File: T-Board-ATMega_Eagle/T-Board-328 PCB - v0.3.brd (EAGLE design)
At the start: 50.8 x 67.9 mm, 26 parts, among them IC1 LD117MIRROR, IC4 NCP1117MIRROR, J1 POWER_JACKPTH, J2 AVR_SPI_PRG_6PTH, U1 ATMEGA328P_PDIP

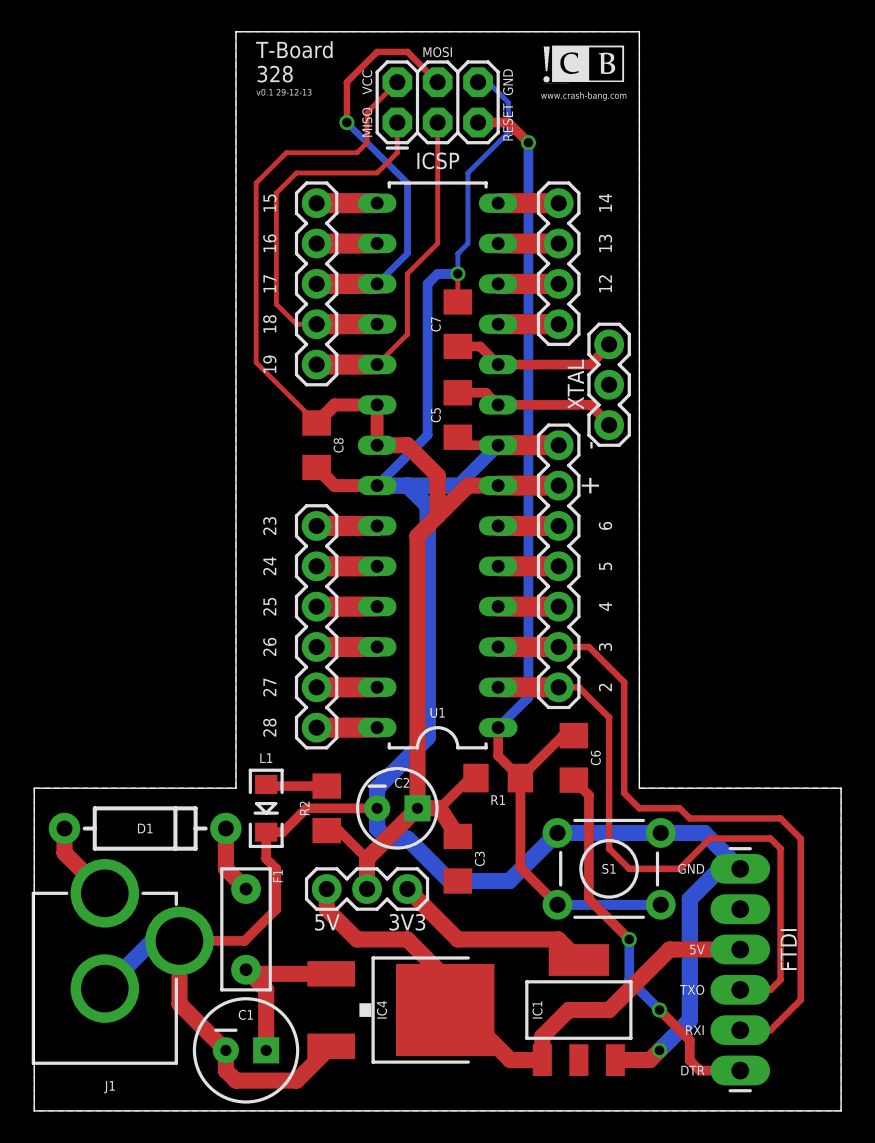
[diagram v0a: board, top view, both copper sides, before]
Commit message: v0.4 - Second Prototype
Second prototype sent to OSHPark for fab.
- Reduced footprint
- Corrected mirrored voltage regulators
- Corrected unconnected capacitor
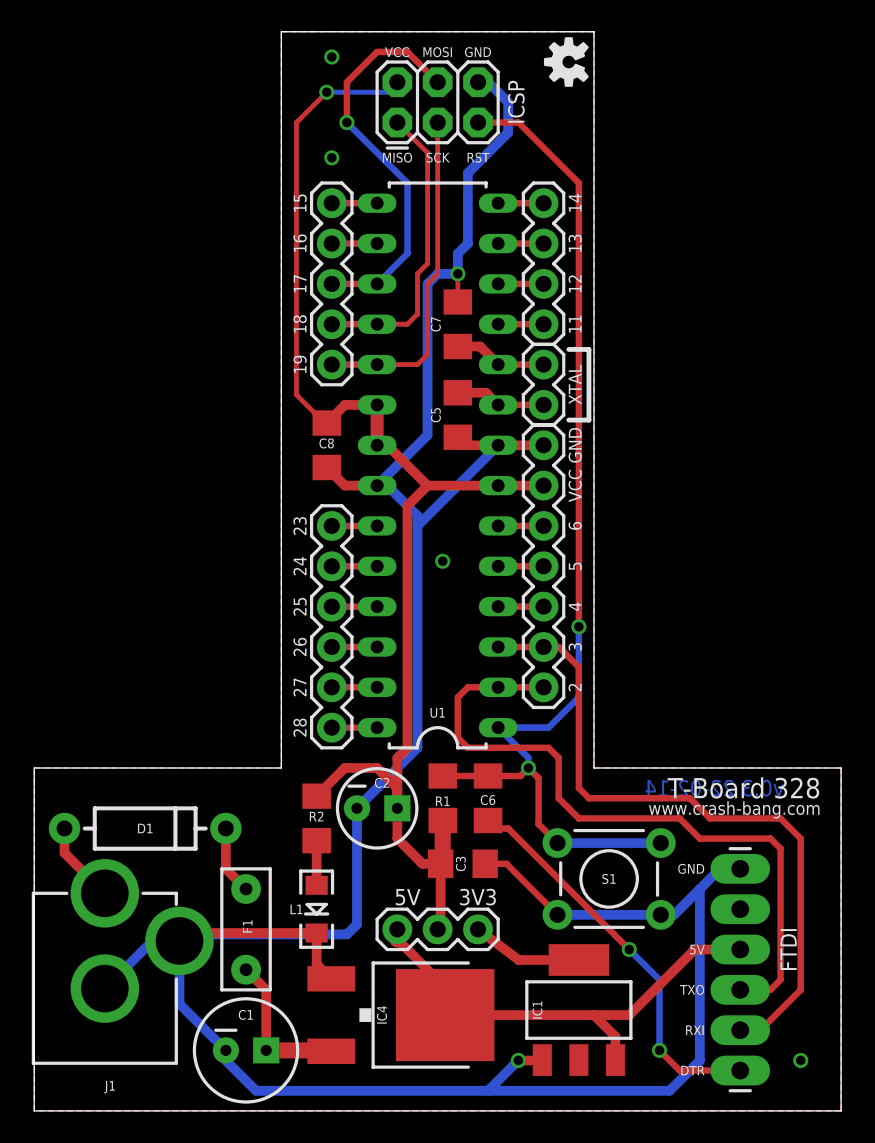
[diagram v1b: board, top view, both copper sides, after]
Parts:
- removed JP10: XTAL, SparkFun-Connectors:1X03
- removed U$1: (no value), CrashBang_Logo:CB_LOGO
- added JP7: XTAL, SparkFun-Connectors:1X02
- added LOGO1: OSHW-LOGOS, SparkFun-Aesthetics:OSHW-LOGO-S
- IC1: value LD117MIRROR -> LD11733TRS
- IC4: value NCP1117MIRROR -> NCP1117DT50GDT
- moved LED1 7.10 mm to (19.1, 12.7)
- moved C6 5.97 mm to (29.8, 19.7)
- moved JP2 5.12 mm to (24.1, 11.4)
- moved R1 3.72 mm to (27.0, 19.7), turned to 270 degrees
- moved C2 1.27 mm to (22.9, 19.1)
- moved JP3 0.95 mm to (33.3, 26.7)
- moved JP4 0.95 mm to (20.0, 57.1)
- moved JP5 0.95 mm to (33.3, 49.5)
- moved JP6 0.95 mm to (20.0, 36.8)
- moved R2 0.90 mm to (19.1, 18.4), turned to 270 degrees
- moved S1 0.63 mm to (37.5, 14.6), turned to 180 degrees
- moved C8 0.63 mm to (19.7, 41.9)
- moved C3 0.45 mm to (28.3, 15.6), turned to 0 degrees
- moved IC4 0.32 mm to (24.8, 6.03)
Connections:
- net 5V: now also IC1.3; no longer IC1.1
- net GND: now also IC1.1, IC4.1; no longer IC1.3, IC4.3
- net N$4: now also IC4.3; no longer IC4.1
- net N$7: now also JP7.1; no longer JP10.1
- net N$8: now also JP7.2; no longer JP10.3
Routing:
- net GND: track 161.9 -> 184.0 mm, vias 2 -> 6
- net 5V: track 36.5 -> 30.3 mm
- net MISO: track 24.4 -> 18.8 mm
- net N$10: track 12.6 -> 7.00 mm
- net RX: track 39.5 -> 44.6 mm
- net N$8: track 10.4 -> 5.71 mm
- net N$7: track 10.6 -> 5.87 mm
- net RESET: track 65.0 -> 67.1 mm, vias 1 -> 2
- net N$4: track 11.1 -> 9.75 mm
- net N$9: track 3.85 -> 2.82 mm
- net VCC: track 86.9 -> 85.9 mm, vias 0 -> 1
- net N$5: track 3.81 -> 2.86 mm
- net N$26: track 3.81 -> 2.86 mm
- net N$25: track 3.81 -> 2.86 mm
- net N$24: track 3.81 -> 2.86 mm
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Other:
- outline, holes or cut-outs redrawn
- board text added: "11"
- board text added: "RST"
- board text added: "SCK"
- board text added: "v0.3 22-02-14"
- board text removed: "+"
- board text removed: "-"
- board text removed: "RESET"
- board text removed: "v0.1 29-12-13"

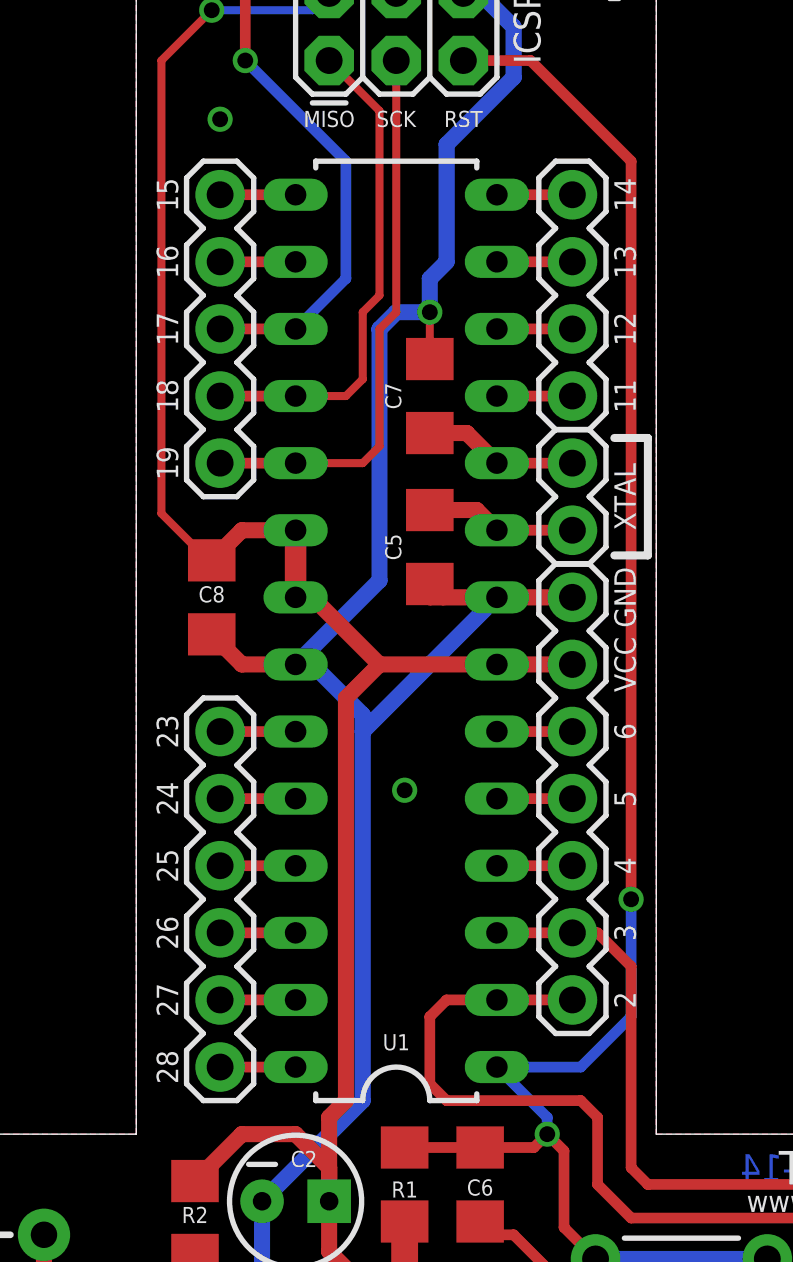
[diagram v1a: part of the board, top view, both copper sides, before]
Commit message: Adjusted header pins
Header pins spacing corrected to fit breadboard more precisely
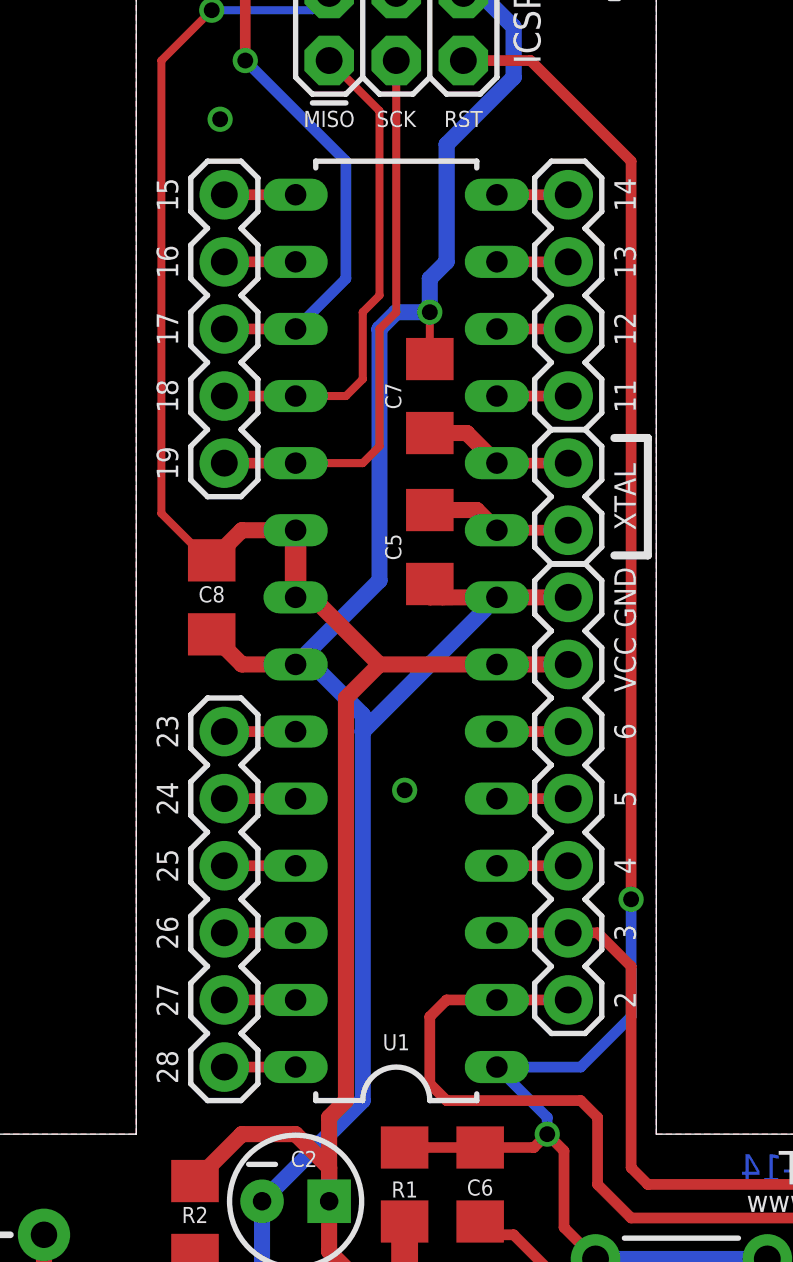
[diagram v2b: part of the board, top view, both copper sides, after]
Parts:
- moved JP3 0.16 mm to (33.2, 26.7)
- moved JP4 0.16 mm to (20.2, 57.1)
- moved JP5 0.16 mm to (33.2, 49.5)
- moved JP6 0.16 mm to (20.2, 36.8)
- moved JP7 0.16 mm to (33.2, 47.0)
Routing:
- net RX: track 44.6 -> 43.8 mm
